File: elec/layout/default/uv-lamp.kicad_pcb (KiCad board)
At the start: 2 copper layers, 40 x 40 mm, 0 parts

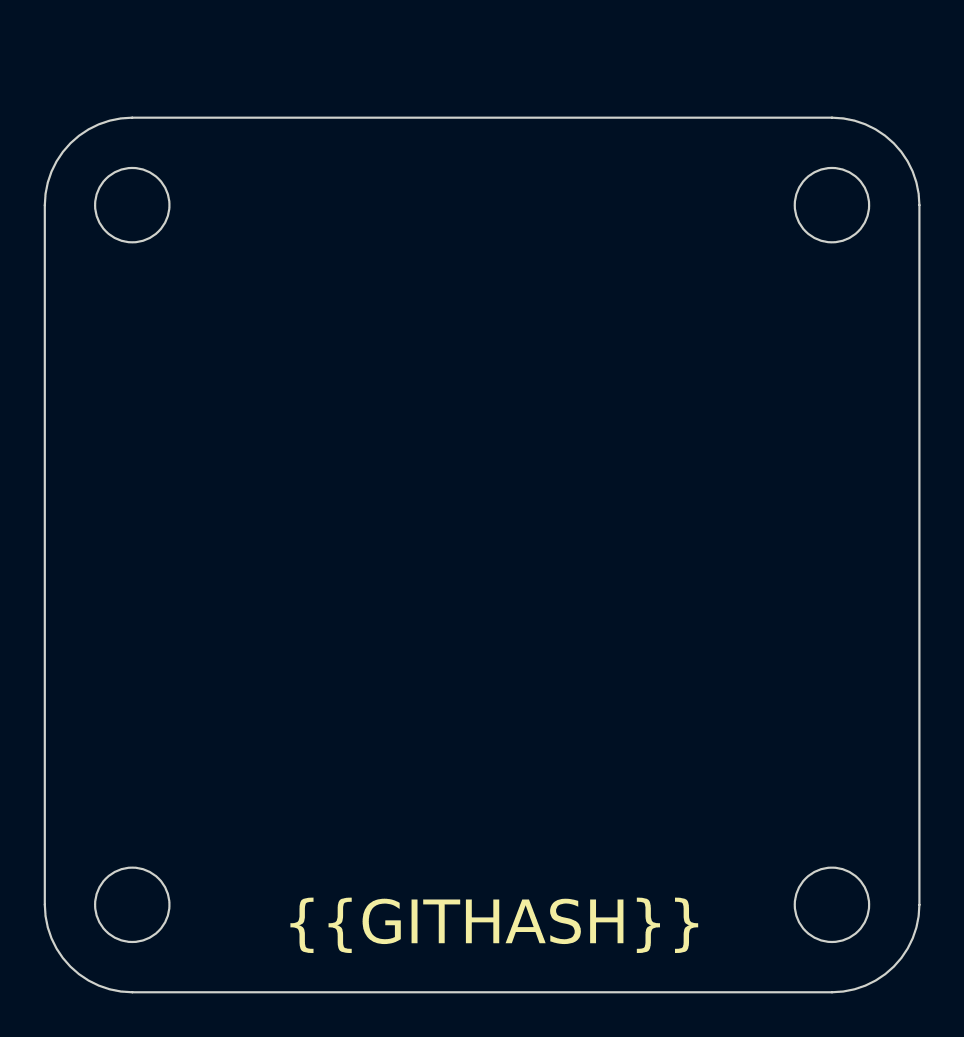
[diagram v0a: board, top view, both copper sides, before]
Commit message: initial commit, ordering diode board to test heatsink fit and thermals
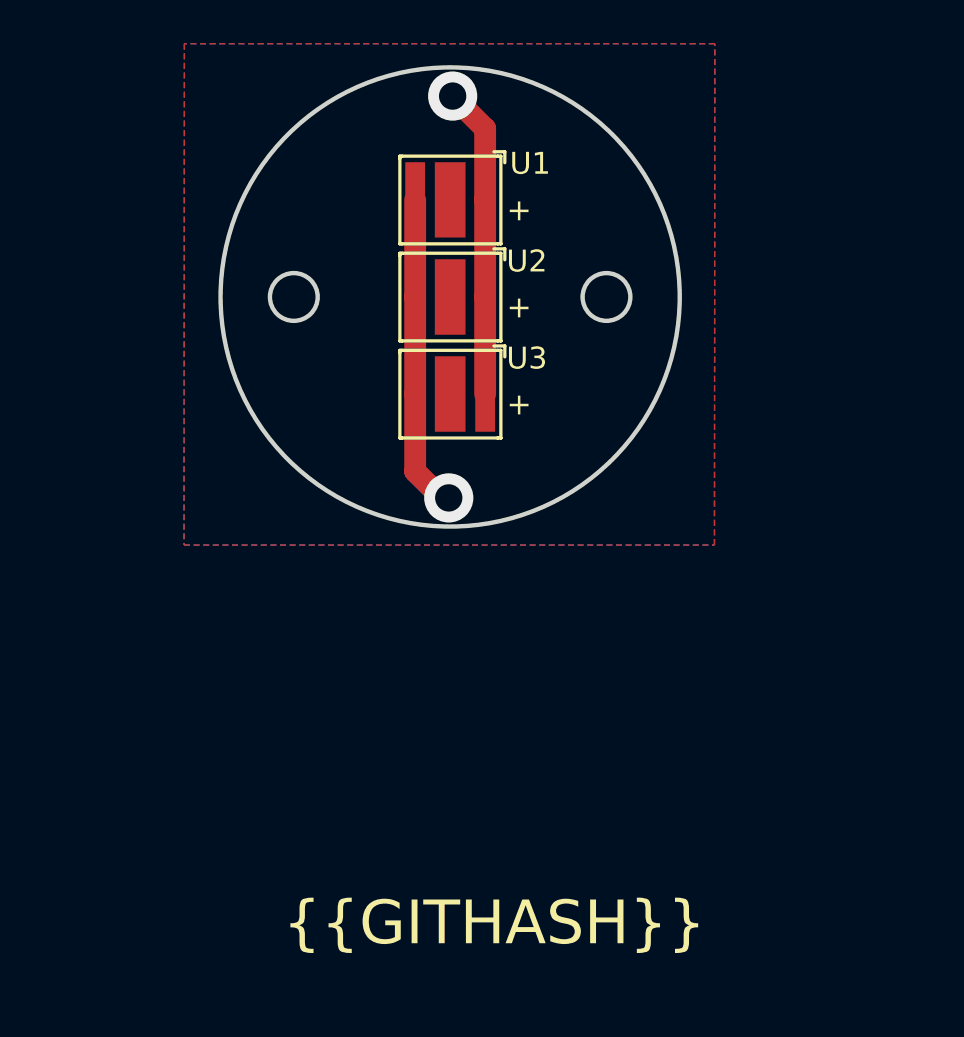
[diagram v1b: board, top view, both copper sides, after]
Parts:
- added U1: ?, lib:LED-SMD_3P-L3.5-W3.5_M3535O1IRS13G06, F.Cu at (147.9, 81.9)
- added U2: ?, lib:LED-SMD_3P-L3.5-W3.5_M3535O1IRS13G06, F.Cu at (147.9, 86.3)
- added U3: ?, lib:LED-SMD_3P-L3.5-W3.5_M3535O1IRS13G06, F.Cu at (147.9, 90.8)
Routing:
- net k: track 0.00 -> 14.5 mm, vias 0 -> 1
- net a: track 0.00 -> 14.2 mm, vias 0 -> 1
- added copper zone on B.Cu, net (none)
- added copper zone on F.Cu, net (none)
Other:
- board size 40 x 40 mm -> 21 x 21 mm
